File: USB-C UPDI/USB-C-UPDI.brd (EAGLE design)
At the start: 30.2 x 21.8 mm, 20 parts, among them IC1 FT232RL, J2 61300511121

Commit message: updates
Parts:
- C1: value 100nf -> 1uf
- C10: value 1uf -> 10uf
- J1: device SparkFun-Connectors:USB-C-16P-2LAYER-PADS -> SparkFun-Connectors:USB-C-16P_4LAYER-PADS
- moved R2 0.64 mm to (28.4, 8.36)
- moved J2 0.47 mm to (24.3, 3.32)
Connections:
- net VCC: now also IC1.19
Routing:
- net VCC: track 47.8 -> 67.3 mm
- net GND: track 73.7 -> 80.3 mm
- net UPDI: track 6.26 -> 9.97 mm
- net N$10: track 16.1 -> 17.0 mm
- net TX: track 21.3 -> 22.1 mm
- net N$3: track 19.5 -> 20.2 mm

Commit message: Updates
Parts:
- C1: value 1uf -> 100nf
- R1: value 1.5k -> 1k
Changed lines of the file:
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@@
 <layer number="14" name="Route14" color="22" fill="1" visible="no" active="no"/>
 <layer number="15" name="Route15" color="23" fill="1" visible="no" active="no"/>
-<layer number="16" name="Bottom" color="1" fill="1" visible="yes" active="yes"/>
+<layer number="16" name="Bottom" color="1" fill="1" visible="no" active="yes"/>
 <layer number="17" name="Pads" color="2" fill="1" visible="yes" active="yes"/>
 <layer number="18" name="Vias" color="2" fill="1" visible="yes" active="yes"/>
@@
 <layer number="20" name="Dimension" color="24" fill="1" visible="yes" active="yes"/>
 <layer number="21" name="tPlace" color="7" fill="1" visible="yes" active="yes"/>
-<layer number="22" name="bPlace" color="7" fill="1" visible="yes" active="yes"/>
+<layer number="22" name="bPlace" color="7" fill="1" visible="no" active="yes"/>
 <layer number="23" name="tOrigins" color="15" fill="1" visible="yes" active="yes"/>
-<layer number="24" name="bOrigins" color="15" fill="1" visible="yes" active="yes"/>
+<layer number="24" name="bOrigins" color="15" fill="1" visible="no" active="yes"/>
 <layer number="25" name="tNames" color="7" fill="1" visible="yes" active="yes"/>
-<layer number="26" name="bNames" color="7" fill="1" visible="yes" active="yes"/>
+<layer number="26" name="bNames" color="7" fill="1" visible="no" active="yes"/>
 <layer number="27" name="tValues" color="7" fill="1" visible="no" active="yes"/>
 <layer number="28" name="bValues" color="7" fill="1" visible="no" active="yes"/>
@@
 <layer number="38" name="bTest" color="7" fill="1" visible="no" active="yes"/>
 <layer number="39" name="tKeepout" color="4" fill="11" visible="yes" active="yes"/>
-<layer number="40" name="bKeepout" color="1" fill="11" visible="yes" active="yes"/>
+<layer number="40" name="bKeepout" color="1" fill="11" visible="no" active="yes"/>
 <layer number="41" name="tRestrict" color="4" fill="10" visible="yes" active="yes"/>
-<layer number="42" name="bRestrict" color="1" fill="10" visible="yes" active="yes"/>
+<layer number="42" name="bRestrict" color="1" fill="10" visible="no" active="yes"/>
 <layer number="43" name="vRestrict" color="2" fill="10" visible="no" active="yes"/>
 <layer number="44" name="Drills" color="7" fill="1" visible="no" active="yes"/>
@@
 <layer number="50" name="dxf" color="7" fill="1" visible="no" active="no"/>
 <layer number="51" name="tDocu" color="7" fill="1" visible="yes" active="yes"/>
-<layer number="52" name="bDocu" color="7" fill="1" visible="yes" active="yes"/>
+<layer number="52" name="bDocu" color="7" fill="1" visible="no" active="yes"/>
 <layer number="53" name="tGND_GNDA" color="7" fill="9" visible="no" active="no"/>
 <layer number="54" name="bGND_GNDA" color="1" fill="9" visible="no" active="no"/>
@@
 <attribute name="VALUE" x="16.4564" y="8.5282" size="0.6096" layer="28" font="vector" ratio="20" rot="MR90" align="top-center"/>
 </element>
-<element name="R1" library="eagle_fab" package="R1206FAB" value="1.5k" x="7.7664" y="3.9782" smashed="yes" rot="MR225">
+<element name="R1" library="eagle_fab" package="R1206FAB" value="1k" x="7.7664" y="3.9782" smashed="yes" rot="MR225">
 <attribute name="NAME" x="5.6111375" y="4.337409375" size="1.016" layer="26" ratio="15" rot="MR225"/>
 <attribute name="VALUE" x="8.125609375" y="6.85188125" size="1.016" layer="28" ratio="15" rot="MR225"/>
 </element>
-<element name="C1" library="01_SparkFun" package="1206" value="1uf" x="25.6654" y="9.9082" smashed="yes" rot="R270">
+<element name="C1" library="01_SparkFun" package="1206" value="100nf" x="25.6654" y="9.9082" smashed="yes" rot="R270">
 <attribute name="NAME" x="26.8084" y="11.1782" size="0.4064" layer="25" rot="R270"/>
 <attribute name="VALUE" x="24.1414" y="11.3052" size="0.4064" layer="27" rot="R270"/>

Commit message: updates
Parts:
- removed C4: 100nf, 01_SparkFun:1206
- removed R3, R4, R7, R8: 10k, 01_SparkFun:1206
- added C2: 100nf, 01_SparkFun:1206
- added D2: SCHOTTKY, eagle_fab:MINI-SMA
- C10: value 10uf -> 4.7uf
- R10, R9: value 100 -> 5.1k
- R5, R6: value 330 -> 1k
- moved TX-LED 55.0 mm to (3.43, -31.5), turned to 0 degrees
- moved RX-LED 46.2 mm to (3.43, -25.4), turned to 0 degrees
- moved C10 20.8 mm to (3.43, -16.5), turned to 0 degrees
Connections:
- removed net N$50: R10.2, R3.2, R7.2
- net GND: now also C2.2; no longer C4.2
- net N$42: now also J1.B5, R10.2; no longer R4.2, R8.2, R9.2
- net N$45: now also TX-LED.2; no longer RX-LED.2
- net N$46: now also RX-LED.2; no longer TX-LED.2
- net N$49: now also C10.1, C2.1, D2.ANODE, J1.VBUS1, J1.VBUS2; no longer J1.B5, R3.1, R7.1
- net N$9: now also R9.2; no longer R4.1, R8.1
- net VCC: now also D2.KATHODE; no longer C10.1, C4.1, J1.VBUS1, J1.VBUS2
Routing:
- net GND: track 80.3 -> 18.2 mm
- net N$50: track 18.8 -> 0.00 mm
- net VCC: track 67.3 -> 53.2 mm
- net N$9: track 9.78 -> 0.00 mm
- net N$42: track 5.60 -> 0.00 mm
- net N$49: track 9.32 -> 4.83 mm

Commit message: programmer updates
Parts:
- moved R2 61.9 mm to (-25.6, -21.8)
- moved D1 42.8 mm to (-25.4, -16.3)
- moved R1 42.8 mm to (-29.9, -16.3)
- moved R9 37.7 mm to (-1.57, -16.3)
- moved R5 36.7 mm to (6.73, -17.6)
- moved C10 36.6 mm to (25.4, 12.8)
- moved R10 36.5 mm to (15.7, -15.1), turned to 90 degrees
- moved R6 36.5 mm to (3.88, -12.9)
- moved C2 29.8 mm to (25.4, -0.13)
- moved D2 29.1 mm to (19.6, 12.8)
- moved J2 23.0 mm to (1.55, 6.58), turned to 270 degrees
- moved C1 18.7 mm to (7.25, 6.55), turned to 90 degrees
- moved J1 15.5 mm to (23.3, 6.41), turned to 90 degrees
- moved RX-LED 14.2 mm to (-9.35, -19.2)
- moved TX-LED 14.1 mm to (-10.5, -33.5)
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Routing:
- net VCC: track 53.2 -> 0.00 mm
- net TX: track 22.1 -> 0.00 mm
- net N$3: track 20.2 -> 0.00 mm
- net GND: track 18.2 -> 0.00 mm
- net N$51: track 17.4 -> 0.00 mm
- net N$10: track 17.0 -> 0.00 mm
- net N$11: track 15.7 -> 0.00 mm
- net N$6: track 14.4 -> 0.00 mm, vias 1 -> 0
- net N$8: track 13.7 -> 0.00 mm, vias 1 -> 0
- net N$61: track 15.2 -> 2.00 mm
- net N$5: track 10.3 -> 0.00 mm
- net N$69: track 12.1 -> 1.88 mm
- net UPDI: track 9.97 -> 0.00 mm
- net N$2: track 9.86 -> 0.00 mm
- net N$7: track 9.80 -> 0.00 mm
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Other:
- board size 30.2 x 21.8 mm -> 5 x 8.6 mm

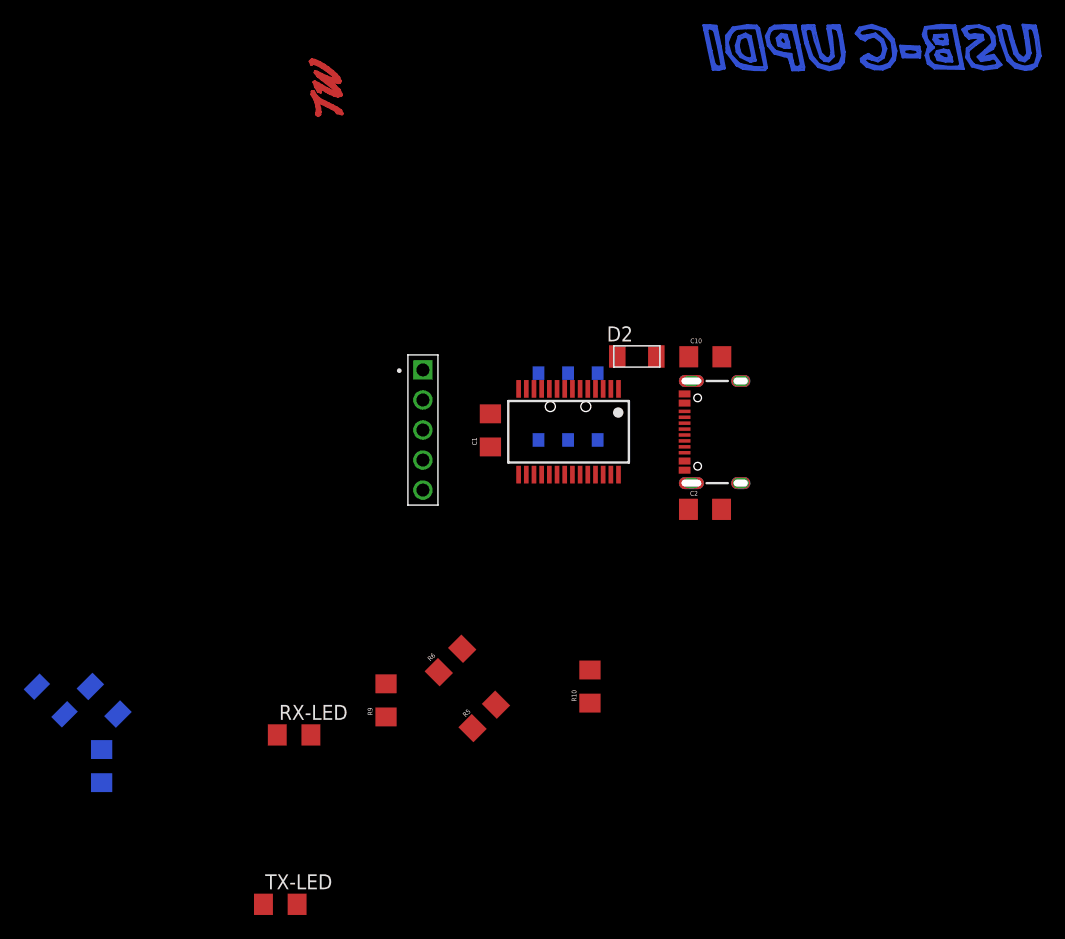
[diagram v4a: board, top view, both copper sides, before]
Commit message: USB-C UPDI Updates
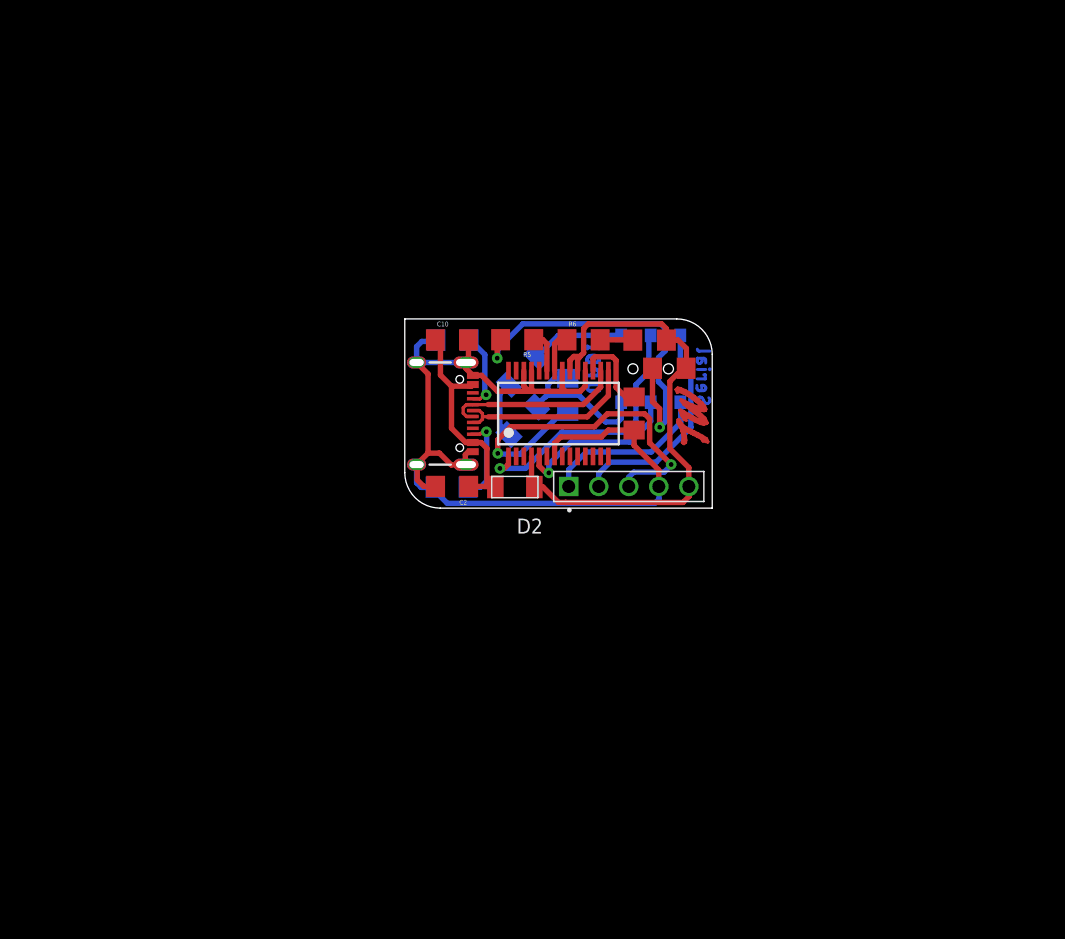
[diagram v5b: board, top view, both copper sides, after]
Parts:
- moved TX-LED 56.0 mm to (22.4, 11.8), turned to 180 degrees
- moved R2 50.4 mm to (13.8, 9.55)
- moved R1 48.7 mm to (9.98, 11.6), turned to 135 degrees
- moved RX-LED 44.9 mm to (20.7, 14.2), turned to 180 degrees
- moved D1 42.6 mm to (9.99, 7.36), turned to 135 degrees
- moved R5 32.0 mm to (9.52, 14.2), turned to 180 degrees
- moved R9 31.0 mm to (4.05, 14.2), flipped to the bottom, turned to 180 degrees
- moved R6 29.4 mm to (15.1, 14.2), turned to 0 degrees
- moved C10 21.5 mm to (4.00, 14.2)
- moved C2 21.5 mm to (4.02, 1.81), turned to 180 degrees
- moved R10 20.5 mm to (3.97, 1.75), flipped to the bottom, turned to 180 degrees
- moved J2 18.0 mm to (19.0, 1.81), turned to 0 degrees
- moved J1 17.3 mm to (6.11, 7.98), turned to 270 degrees
- moved D2 15.1 mm to (9.32, 1.76), turned to 180 degrees
- moved C1 12.2 mm to (19.4, 7.98), turned to 270 degrees
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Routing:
- net GND: track 0.00 -> 84.5 mm
- net VCC: track 0.00 -> 47.3 mm
- net N$45: track 0.00 -> 32.4 mm, vias 0 -> 2
- net UPDI: track 0.00 -> 32.0 mm, vias 0 -> 2
- net N$10: track 0.00 -> 22.1 mm, vias 0 -> 1
- net N$49: track 0.00 -> 18.9 mm
- net TX: track 0.00 -> 18.7 mm
- net N$64: track 17.6 -> 0.00 mm
- net N$52: track 17.4 -> 0.00 mm
- net N$54: track 15.6 -> 0.00 mm
- net N$53: track 15.6 -> 0.00 mm
- net N$65: track 15.5 -> 0.00 mm
- net N$2: track 0.00 -> 15.5 mm
- net N$62: track 15.2 -> 0.00 mm
- net RX: track 0.00 -> 14.3 mm
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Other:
- board size 5 x 8.6 mm -> 26 x 16 mm
